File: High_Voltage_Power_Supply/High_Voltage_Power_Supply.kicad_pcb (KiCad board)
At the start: 2 copper layers, 127 x 102.9 mm, 41 parts, among them J1 Conn_01x02_Female, J2 Conn_01x02_Female, J3 Conn_01x02_Female, J4 Conn_01x02_Female, J5 Conn_01x02_Female, J6 Conn_01x02_Female, Q1 Q_NMOS_GDS, U1 LT3751-TSSOP

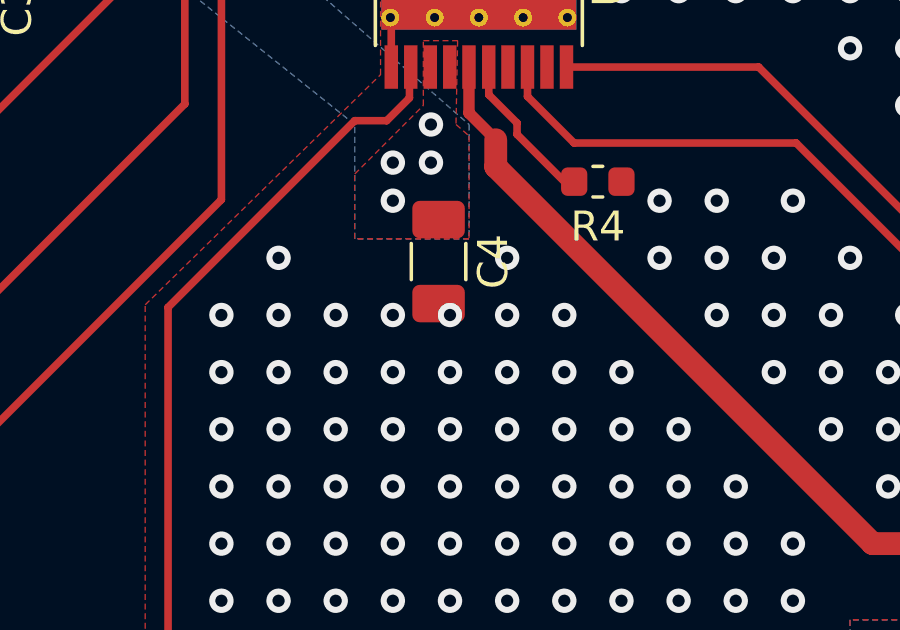
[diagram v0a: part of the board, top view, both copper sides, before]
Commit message: Removed a via in the wrong position
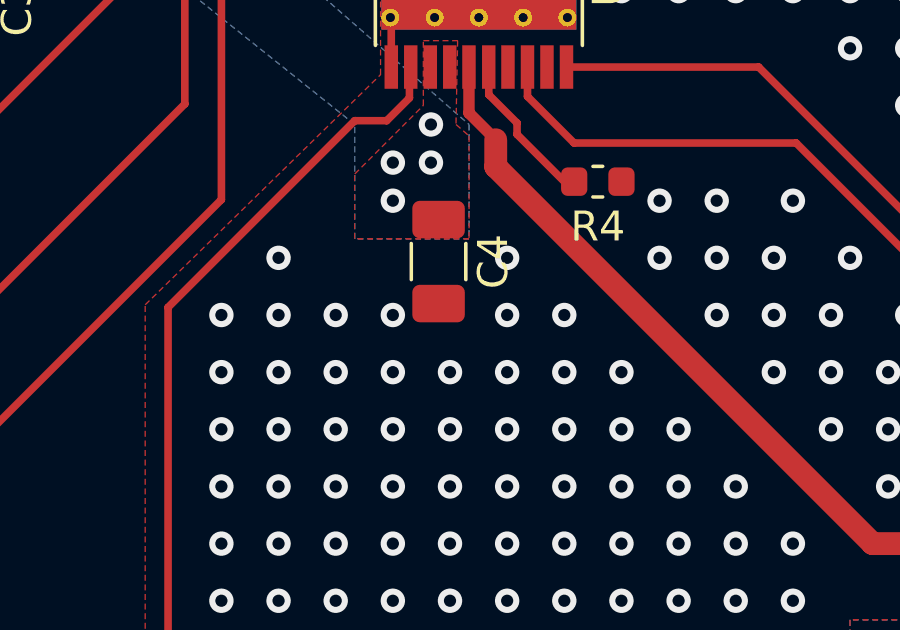
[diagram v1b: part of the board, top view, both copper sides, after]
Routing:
- net GND: vias 709 -> 708

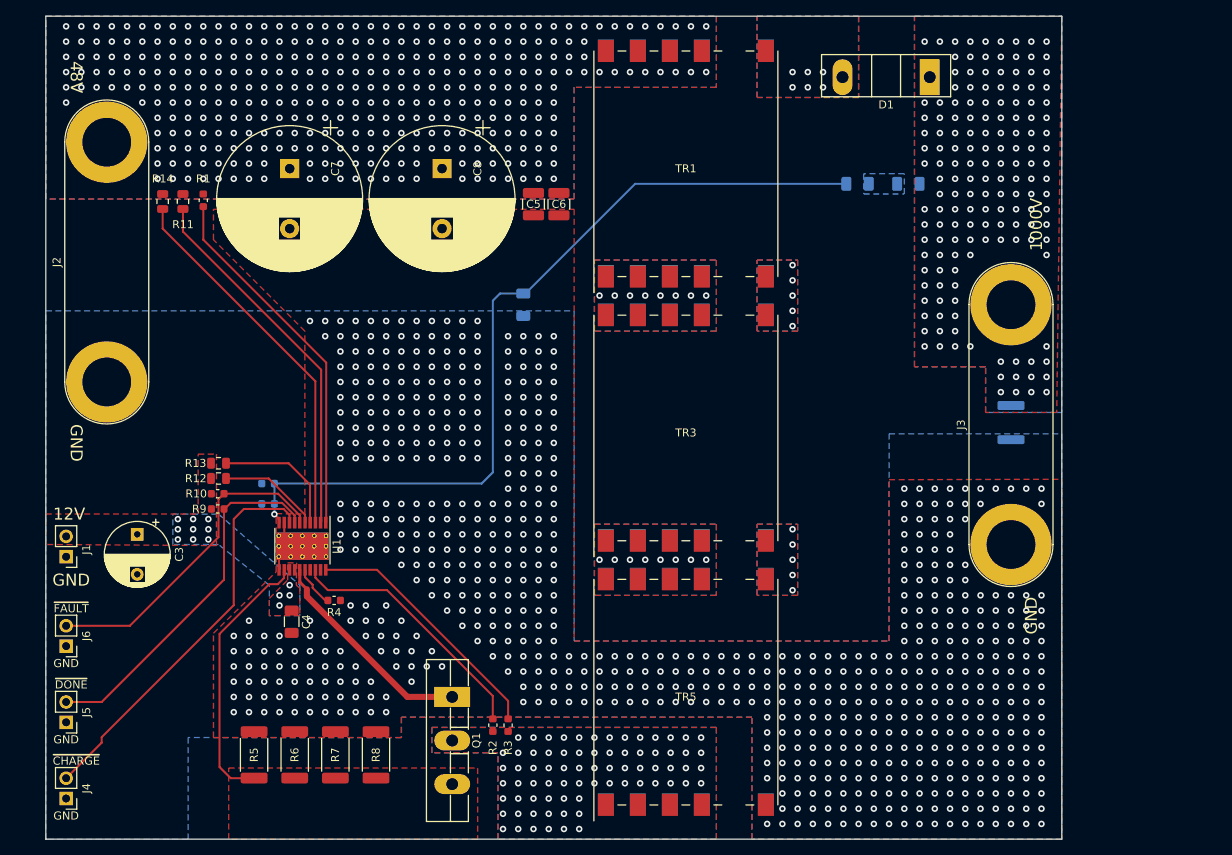
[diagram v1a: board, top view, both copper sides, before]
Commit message: Updated schematic to run on regulation mode only
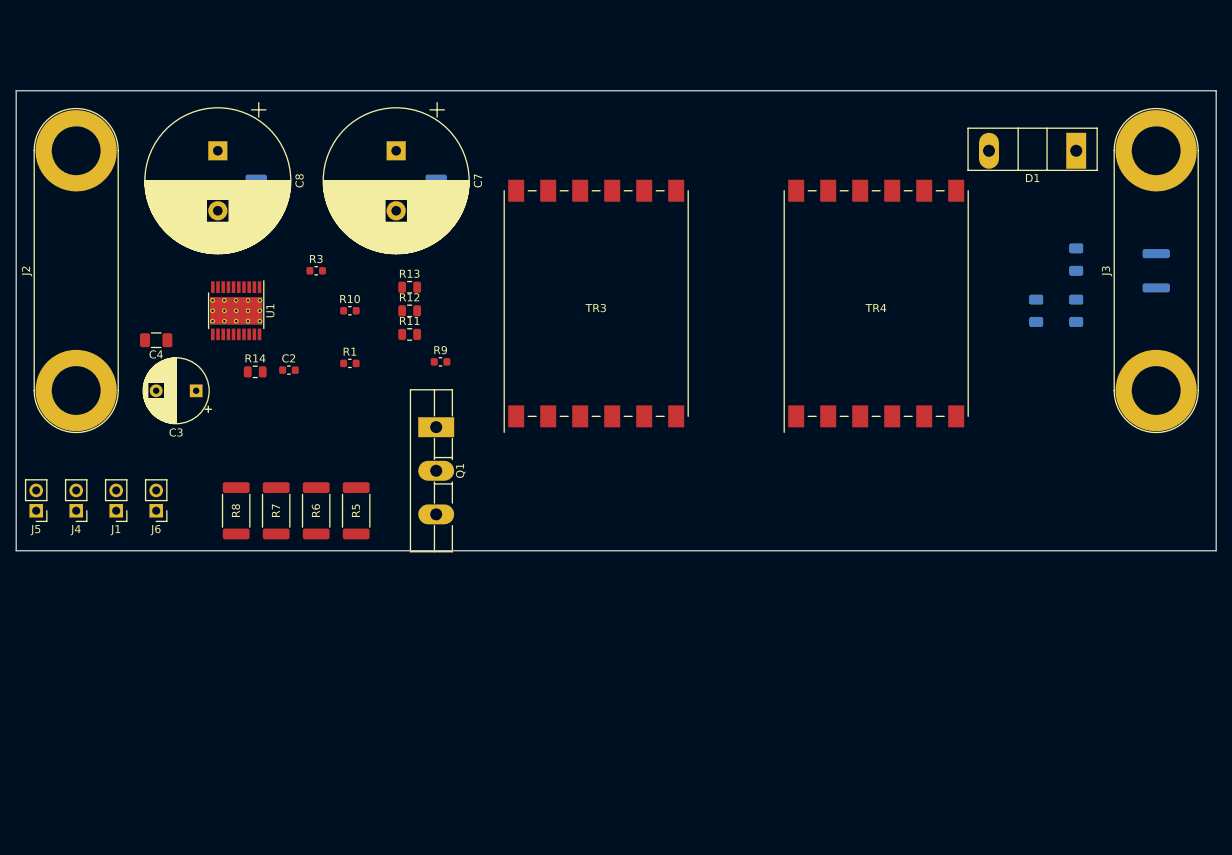
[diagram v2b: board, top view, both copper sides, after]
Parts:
- removed JP1: Jumper_2_Open, Resistor_SMD:R_0603_1608Metric
- removed R2: 80.6k, Resistor_SMD:R_0603_1608Metric
- removed R4: 681, Resistor_SMD:R_0603_1608Metric
- removed TR1, TR2, TR5, TR6: GA3460-BL, High_Voltage_Power_Supply:Transformer_Coilcraft_GA3460-BL
- C2, TR4: moved to F.Cu
- C5, C6: moved to B.Cu
- moved R17 64.1 mm to (200.0, 80.0), turned to 90 degrees
- moved R3 61.7 mm to (110.0, 75.0), turned to 0 degrees
- moved C4 39.1 mm to (90.0, 83.7), turned to 180 degrees
- moved J4 36.0 mm to (80.0, 105.0)
- moved R8 35.2 mm to (100.0, 105.0)
- moved C5 34.7 mm to (102.5, 65.0)
- moved Q1 33.8 mm to (125.0, 94.5)
- moved R9 33.4 mm to (125.5, 86.4), turned to 0 degrees
- moved R5 33.1 mm to (115.0, 105.0)
- moved R11 32.8 mm to (121.7, 83.0), turned to 0 degrees
- moved R13 32.5 mm to (121.7, 77.1), turned to 0 degrees
- moved R12 31.8 mm to (121.7, 80.0), turned to 0 degrees
- moved R16 31.6 mm to (205.0, 80.0), turned to 270 degrees
- moved R7 31.4 mm to (105.0, 105.0)
- moved R6 30.6 mm to (110.0, 105.0)
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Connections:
- TR3 pad 1: Net-(TR3-Pad1) -> /Transformer/in-
- TR3 pad 10: Net-(TR1-Pad1) -> Vtrans
- TR3 pad 11: Net-(TR1-Pad1) -> Vtrans
- TR3 pad 12: Net-(TR1-Pad1) -> Vtrans
- TR3 pad 2: Net-(TR3-Pad1) -> /Transformer/in-
- TR3 pad 3: Net-(TR3-Pad1) -> /Transformer/in-
- TR3 pad 4: Net-(TR3-Pad1) -> /Transformer/in-
- TR3 pad 6: Net-(TR3-Pad6) -> GND
- TR3 pad 7: Net-(TR1-Pad6) -> /Transformer/out+
- TR3 pad 9: Net-(TR1-Pad1) -> Vtrans
- TR4 pad 1: Net-(TR1-Pad1) -> /Transformer/in-
- TR4 pad 10: Net-(TR3-Pad1) -> Vtrans
- TR4 pad 11: Net-(TR3-Pad1) -> Vtrans
- TR4 pad 12: Net-(TR3-Pad1) -> Vtrans
- TR4 pad 2: Net-(TR1-Pad1) -> /Transformer/in-
- TR4 pad 3: Net-(TR1-Pad1) -> /Transformer/in-
- TR4 pad 4: Net-(TR1-Pad1) -> /Transformer/in-
- TR4 pad 6: Net-(TR1-Pad6) -> GND
- TR4 pad 7: Net-(TR3-Pad6) -> /Transformer/out+
- TR4 pad 9: Net-(TR3-Pad1) -> Vtrans
- U1 pad 16: Net-(R4-Pad1) -> GND
- U1 pad 18: Net-(R2-Pad1) -> GND
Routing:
- net Net-(C2-Pad1): track 103.5 -> 0.00 mm, vias 1 -> 0
- net Net-(J4-Pad2): track 49.8 -> 0.00 mm
- net Net-(R14-Pad1): track 47.1 -> 0.00 mm
- net Net-(R11-Pad1): track 46.3 -> 0.00 mm
- net Net-(R1-Pad2): track 45.8 -> 0.00 mm
- net ~DONE~: track 45.6 -> 0.00 mm
- net ~FAULT~: track 40.9 -> 0.00 mm
- net Net-(Q1-Pad3): track 33.5 -> 0.00 mm
- net Net-(R2-Pad1): track 32.2 -> 0.00 mm
- net Net-(R3-Pad2): track 31.9 -> 0.00 mm
- net Net-(Q1-Pad1): track 27.1 -> 0.00 mm
- net Net-(R13-Pad1): track 16.3 -> 0.00 mm
- net Net-(R12-Pad1): track 12.5 -> 0.00 mm
- net Net-(R4-Pad1): track 4.86 -> 0.00 mm
- net GND: track 3.27 -> 0.00 mm, vias 708 -> 0
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- removed copper zone on B.Cu, net /Transformer/in-
- removed copper zone on F.Cu, net /Transformer/in-
- removed copper zone on B.Cu, net /Transformer/out+
- removed copper zone on F.Cu, net /Transformer/out+
- removed copper zone on B.Cu, net GND
- removed copper zone on F.Cu, net GND
- removed copper zone on B.Cu, net Net-(C1-Pad1)
- removed copper zone on F.Cu, net Net-(C1-Pad1)
- removed copper zone on F.Cu, net Net-(Q1-Pad3)
- removed copper zone on B.Cu, net Net-(R15-Pad2)
- removed copper zone on B.Cu, net Net-(TR1-Pad1)
- removed copper zone on F.Cu, net Net-(TR1-Pad1)
- removed copper zone on B.Cu, net Net-(TR1-Pad6)
- removed copper zone on F.Cu, net Net-(TR1-Pad6)
- removed copper zone on B.Cu, net Net-(TR3-Pad1)
- removed copper zone on F.Cu, net Net-(TR3-Pad1)
- removed copper zone on B.Cu, net Net-(TR3-Pad6)
- removed copper zone on F.Cu, net Net-(TR3-Pad6)
- removed copper zone on B.Cu, net VCC
- removed copper zone on F.Cu, net VCC
- removed copper zone on B.Cu, net Vtrans
- removed copper zone on F.Cu, net Vtrans
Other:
- board size 127 x 102.9 mm -> 150 x 57.5 mm
- board text removed: "1000V"
- board text removed: "12V"
- board text removed: "48V"
- board text removed: "Corwin Hansen corwinh.com/git akerunakayama@gmail.com (206) 462-8204"
- board text removed: "GND"
- board text removed: "~CHARGE~"
- board text removed: "~DONE~"
- board text removed: "~FAULT~"

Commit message: Started PCB layout for new version of the board
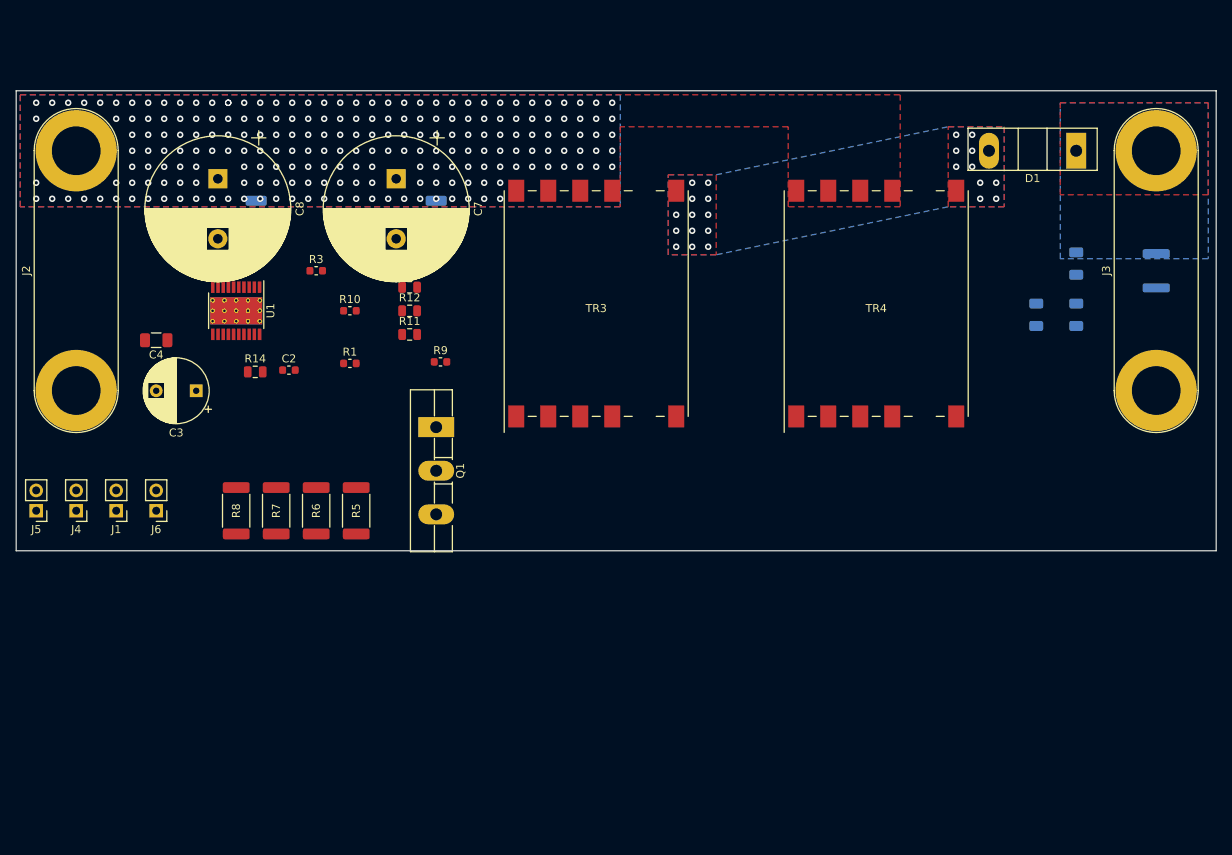
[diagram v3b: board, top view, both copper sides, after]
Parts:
- moved C7 3.50 mm to (120.0, 63.5)
- moved C8 3.50 mm to (97.7, 63.5)
- moved C5 2.65 mm to (102.5, 67.7)
- moved C6 2.65 mm to (125.0, 67.7)
- moved R15 0.50 mm to (205.0, 74.1)
- moved R16 0.50 mm to (205.0, 80.5)
- moved R17 0.50 mm to (200.0, 80.5)
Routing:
- net Vtrans: vias 0 -> 212
- net /Transformer/out+: vias 0 -> 23
- added copper zone on B.Cu, net /Transformer/out+
- added copper zone on F.Cu, net /Transformer/out+
- added copper zone on B.Cu, net Net-(C1-Pad1)
- added copper zone on F.Cu, net Net-(C1-Pad1)
- added copper zone on B.Cu, net Vtrans
- added copper zone on F.Cu, net Vtrans

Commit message: did more pcb layout
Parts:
- moved R17 45.6 mm to (154.4, 82.0), turned to 180 degrees
- moved C1 3.00 mm to (212.0, 75.0)
- moved D1 3.00 mm to (202.0, 60.0)
- moved J3 3.00 mm to (212.0, 90.0)
- moved R15 3.00 mm to (202.0, 74.1)
- moved R16 3.00 mm to (202.0, 80.5)
- moved TR4 3.00 mm to (177.0, 79.7)
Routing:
- net GND: vias 0 -> 26
- added copper zone on F.Cu, net /Transformer/in-
- added copper zone on B.Cu, net GND
- added copper zone on F.Cu, net GND
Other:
- board size 150 x 57.5 mm -> 147 x 57.5 mm
